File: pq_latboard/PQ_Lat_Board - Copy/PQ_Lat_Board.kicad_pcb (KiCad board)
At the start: 6 copper layers, 48 x 48 mm, 27 parts, among them IC1 TCN75AVOA713, J1 Conn_01x11_MountingPin, J2 Conn_Coaxial

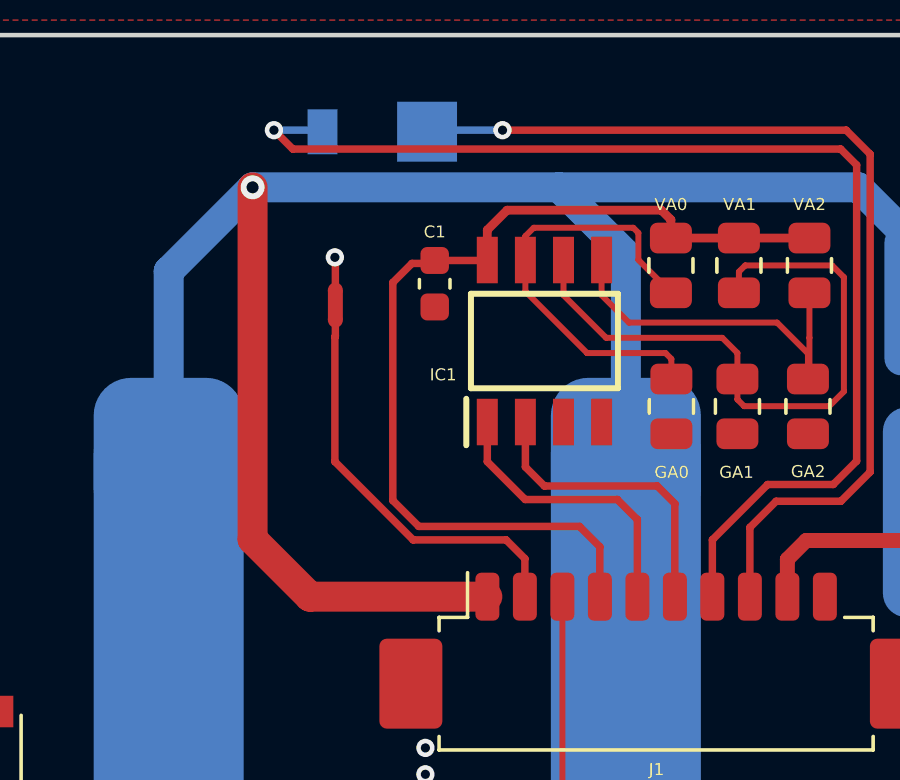
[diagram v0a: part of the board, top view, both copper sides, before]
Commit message: LAteral no photodiode finished
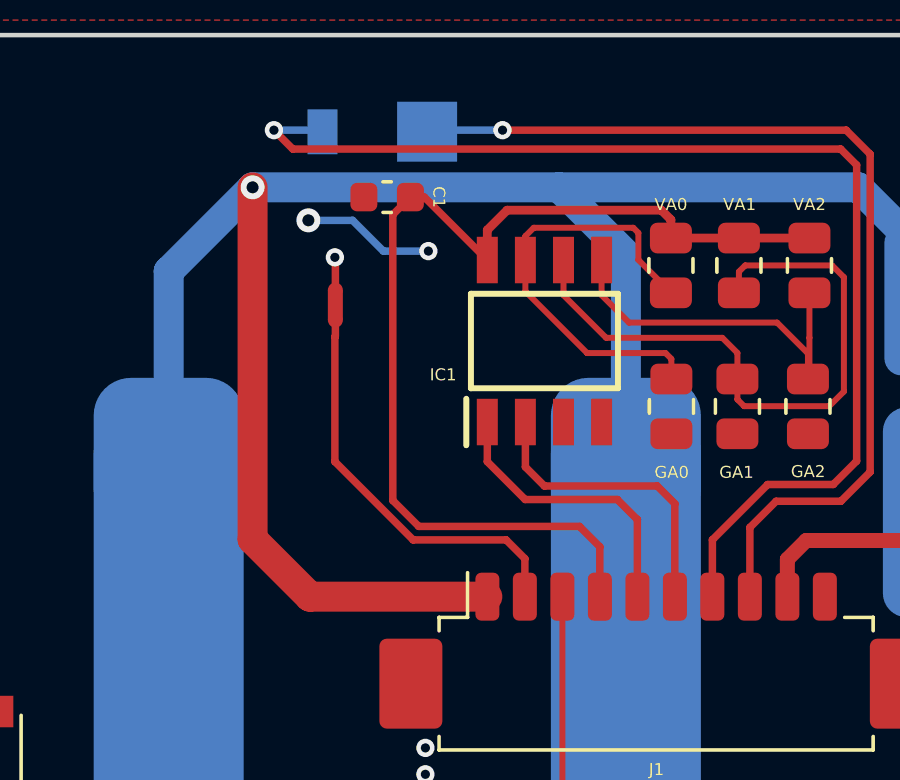
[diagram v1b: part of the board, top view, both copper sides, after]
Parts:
- moved C1 3.29 mm to (97.9, 47.4), turned to 180 degrees
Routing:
- net GND: track 0.00 -> 4.42 mm, vias 11 -> 13
- net /VCC: track 32.6 -> 35.8 mm
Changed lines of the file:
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@@
 	(footprint "Capacitor_SMD:C_0603_1608Metric"
 		(layer "F.Cu")
-		(at 99.511 50.2874 -90)
+		(at 97.925 47.4 180)
 		(descr "Capacitor SMD 0603 (1608 Metric), square (rectangular) end terminal, IPC_7351 nominal, (Body size source: IPC-SM-782 page 76, https://www.pcb-3d.com/wordpress/wp-content/uploads/ipc-sm-782a_amendment_1_and_2.pdf), generated with kicad-footprint-generator")
 		(tags "capacitor")
 		(property "Reference" "C1"
-			(at -1.7272 0 0)
+			(at -1.7272 0 270)
 			(unlocked yes)
 			(layer "F.SilkS")
@@
 		)
 		(property "Value" "1 uF"
-			(at 0 1.43 90)
+			(at 0 1.43 0)
 			(layer "F.Fab")
 			(effects
@@
 		)
 		(property "Datasheet" "~"
-			(at 0 0 270)
+			(at 0 0 0)
 			(layer "F.Fab")
 			(hide yes)
@@
 		)
 		(property "Description" ""
-			(at 0 0 270)
+			(at 0 0 0)
 			(layer "F.Fab")
 			(hide yes)
@@
 		)
 		(property "Manufacturer 1" "Murata Electronics"
-			(at 49.2236 149.7984 0)
+			(at 49.2236 149.7984 90)
 			(layer "F.Fab")
 			(hide yes)
@@
 		)
 		(property "Manufacturer Part Number 1" "GRM188R72A104KA35J"
-			(at 49.2236 149.7984 0)
+			(at 49.2236 149.7984 90)
 			(layer "F.Fab")
 			(hide yes)
@@
 		)
 		(property "Supplier 1" "Mouser"
-			(at 49.2236 149.7984 0)
+			(at 49.2236 149.7984 90)
 			(layer "F.Fab")
 			(hide yes)
@@
 		)
 		(property "Supplier Part Number 1" "81-GRM188R72A104KA5J"
-			(at 49.2236 149.7984 0)
+			(at 49.2236 149.7984 90)
 			(layer "F.Fab")
 			(hide yes)
@@
 		)
 		(fp_line
-			(start -1.48 0.73)
-			(end -1.48 -0.73)
+			(start 1.48 0.73)
+			(end -1.48 0.73)
 			(stroke
 				(width 0.05)
@@
 		)
 		(fp_line
-			(start 1.48 0.73)
-			(end -1.48 0.73)
+			(start 1.48 -0.73)
+			(end 1.48 0.73)
 			(stroke
 				(width 0.05)
@@
 		)
 		(fp_line
-			(start -1.48 -0.73)
-			(end 1.48 -0.73)
+			(start -1.48 0.73)
+			(end -1.48 -0.73)
 			(stroke
 				(width 0.05)
@@
 		)
 		(fp_line
-			(start 1.48 -0.73)
-			(end 1.48 0.73)
+			(start -1.48 -0.73)
+			(end 1.48 -0.73)
 			(stroke
 				(width 0.05)
@@
 		)
 		(fp_line
-			(start -0.8 0.4)
-			(end -0.8 -0.4)
+			(start 0.8 0.4)
+			(end -0.8 0.4)
 			(stroke
 				(width 0.1)
@@
 		)
 		(fp_line
-			(start 0.8 0.4)
-			(end -0.8 0.4)
+			(start 0.8 -0.4)
+			(end 0.8 0.4)
 			(stroke
 				(width 0.1)
@@
 		)
 		(fp_line
-			(start -0.8 -0.4)
-			(end 0.8 -0.4)
+			(start -0.8 0.4)
+			(end -0.8 -0.4)
 			(stroke
 				(width 0.1)
@@
 		)
 		(fp_line
-			(start 0.8 -0.4)
-			(end 0.8 0.4)
+			(start -0.8 -0.4)
+			(end 0.8 -0.4)
 			(stroke
 				(width 0.1)
@@
 		)
 		(fp_text user "${REFERENCE}"
-			(at 0 0 90)
+			(at 0 0 0)
 			(layer "F.Fab")
 			(effects
@@
 		)
 		(pad "1" smd roundrect
-			(at -0.775 0 270)
+			(at -0.775 0 180)
 			(size 0.9 0.95)
 			(layers "F.Cu" "F.Mask" "F.Paste")
@@
 		)
 		(pad "2" smd roundrect
-			(at 0.775 0 270)
+			(at 0.775 0 180)
 			(size 0.9 0.95)
 			(layers "F.Cu" "F.Mask" "F.Paste")
@@
 	)
 	(segment
-		(start 104.337 58.377)
-		(end 105.016617 59.056617)
-		(width 0.25)
+		(start 109.651 48.7653)
+		(end 112.002 48.7653)
+		(width 0.293)
 		(layer "F.Cu")
 		(net 3)
 	)
 	(segment
-		(start 98.978996 58.377)
-		(end 104.337 58.377)
+		(start 104.337 58.377)
+		(end 98.978996 58.377)
 		(width 0.25)
 		(layer "F.Cu")
@@
 	)
 	(segment
-		(start 109.651 48.7653)
-		(end 112.002 48.7653)
-		(width 0.293)
+		(start 105.016617 59.056617)
+		(end 104.337 58.377)
+		(width 0.25)
 		(layer "F.Cu")
 		(net 3)
@@
 	)
 	(segment
-		(start 101.924 47.836)
-		(end 101.2636 48.4964)
-		(width 0.293)
+		(start 99.1664 47.4)
+		(end 98.7 47.4)
+		(width 0.25)
 		(layer "F.Cu")
 		(net 3)
 	)
 	(segment
-		(start 98.114 57.512004)
-		(end 98.978996 58.377)
-		(width 0.25)
+		(start 101.924 47.836)
+		(end 101.2636 48.4964)
+		(width 0.293)
 		(layer "F.Cu")
 		(net 3)
@@
 	)
 	(segment
-		(start 105.016617 59.056617)
-		(end 105.016617 60.718784)
-		(width 0.25)
+		(start 107.385 48.7653)
+		(end 109.651 48.7653)
+		(width 0.293)
 		(layer "F.Cu")
 		(net 3)
 	)
 	(segment
-		(start 107.385 48.7653)
-		(end 109.651 48.7653)
-		(width 0.293)
+		(start 98.114 57.512004)
+		(end 98.114 47.986)
+		(width 0.25)
 		(layer "F.Cu")
 		(net 3)
@@
 	)
 	(segment
-		(start 99.511 49.5124)
-		(end 101.2484 49.5124)
+		(start 98.114 47.986)
+		(end 98.7 47.4)
 		(width 0.25)
 		(layer "F.Cu")
@@
 	)
 	(segment
-		(start 98.114 50.249)
+		(start 98.978996 58.377)
 		(end 98.114 57.512004)
 		(width 0.25)
@@
 	)
 	(segment
-		(start 98.7526 49.6104)
-		(end 98.114 50.249)
+		(start 105.016617 60.718784)
+		(end 105.016617 59.056617)
 		(width 0.25)
 		(layer "F.Cu")
@@
 	)
 	(segment
-		(start 99.4614 49.6104)
-		(end 98.7526 49.6104)
+		(start 101.2636 49.4972)
+		(end 99.1664 47.4)
 		(width 0.25)
 		(layer "F.Cu")
@@
 	)
 	(via
+		(at 99.3 49.2)
+		(size 0.61)
+		(drill 0.305)
+		(layers "F.Cu" "B.Cu")
+		(net 9)
+	)
+	(via
 		(at 115.767 75.2934)
 		(size 0.61)
@@
 	)
 	(via
+		(at 95.3 48.174)
+		(size 0.8)
+		(drill 0.4)
+		(layers "F.Cu" "B.Cu")
+		(net 9)
+	)
+	(via
 		(at 117.6974 60.7392)
 		(size 0.61)
@@
 		(net 9)
 	)
+	(segment
+		(start 95.3 48.174)
+		(end 96.774 48.174)
+		(width 0.25)
+		(layer "B.Cu")
+		(net 9)
+	)
+	(segment
+		(start 97.8 49.2)
+		(end 99.3 49.2)
+		(width 0.25)
+		(layer "B.Cu")
+		(net 9)
+	)
+	(segment
+		(start 96.774 48.174)
+		(end 97.8 49.2)
+		(width 0.25)
+		(layer "B.Cu")
+		(net 9)
+	)
